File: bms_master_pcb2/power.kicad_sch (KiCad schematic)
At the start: 10 parts, among them U501 AP63205WU, U502 AP2112K-3.3

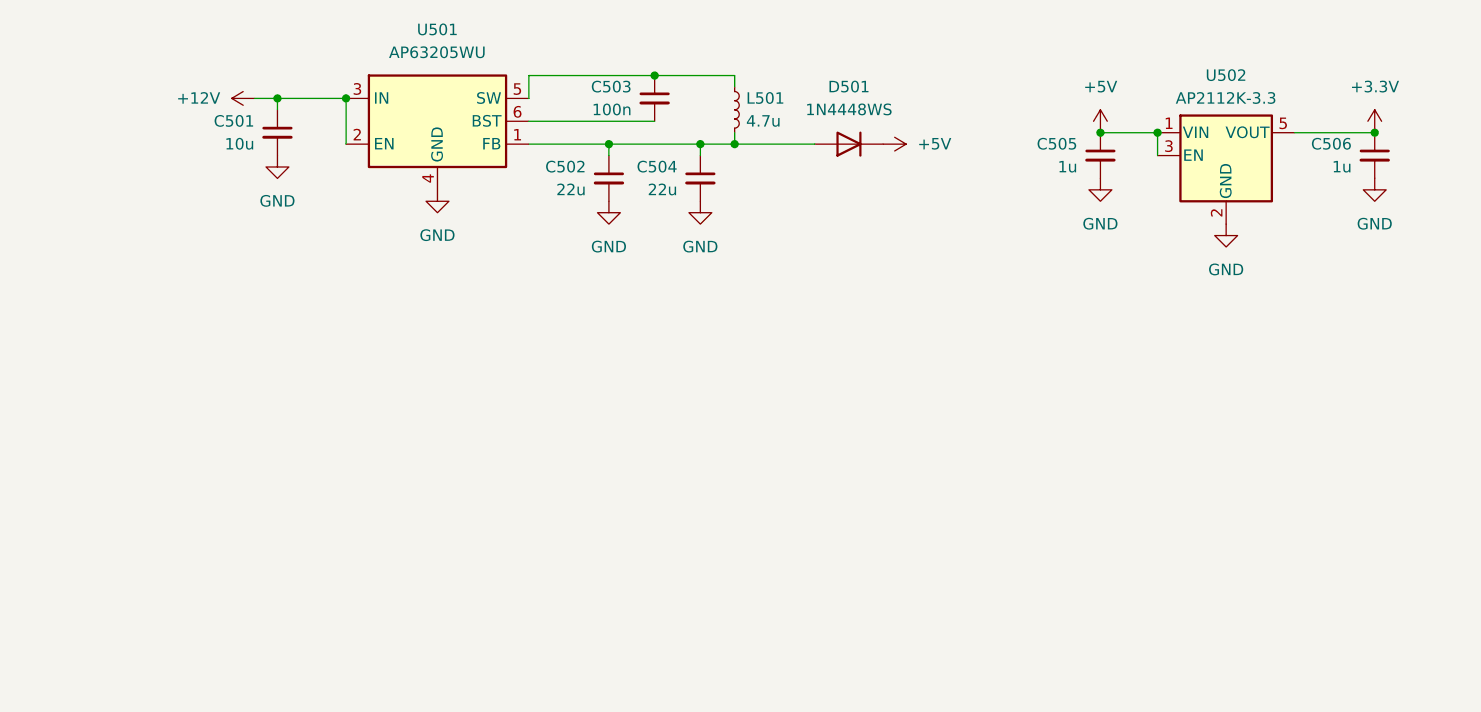
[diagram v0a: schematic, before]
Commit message: Add files via upload
almost done with the PCB layout. Harrison needs to fix routing on the differential pairs
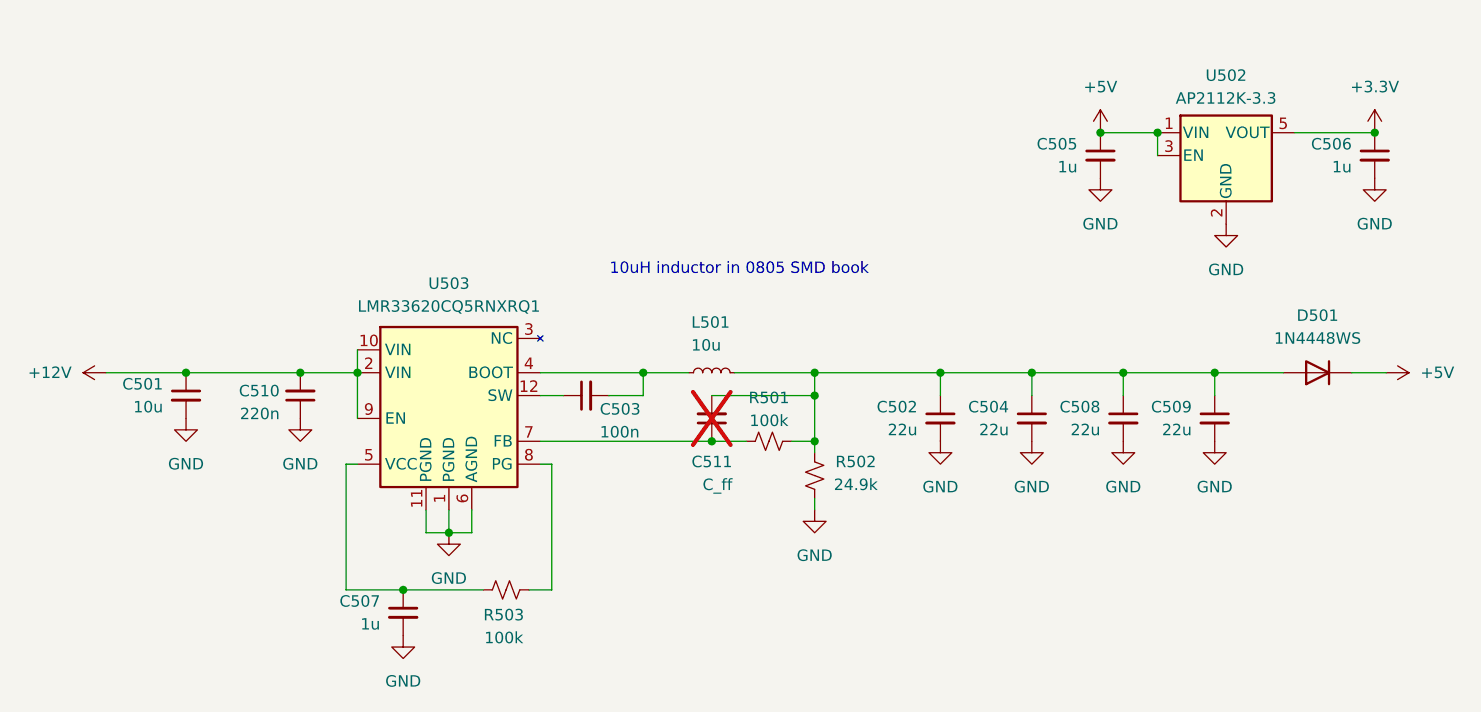
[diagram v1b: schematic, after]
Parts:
- removed U501: AP63205WU, Package_TO_SOT_SMD:TSOT-23-6, symbol Regulator_Switching:AP63205WU
- added C507: 1u, Capacitor_SMD:C_0805_2012Metric_Pad1.18x1.45mm_HandSolder, symbol Device:C_Small
- added C508, C509: 22u, Capacitor_SMD:C_0805_2012Metric_Pad1.18x1.45mm_HandSolder, symbol Device:C_Small
- added C510: 220n, Capacitor_SMD:C_0603_1608Metric_Pad1.08x0.95mm_HandSolder, symbol Device:C_Small
- added C511: C_ff, Capacitor_SMD:C_0603_1608Metric_Pad1.08x0.95mm_HandSolder, symbol Device:C_Small
- added R501, R503: 100k, Resistor_SMD:R_0603_1608Metric_Pad0.98x0.95mm_HandSolder, symbol Device:R_Small_US
- added R502: 24.9k, Resistor_SMD:R_0603_1608Metric_Pad0.98x0.95mm_HandSolder, symbol Device:R_Small_US
- added U503: LMR33620CQ5RNXRQ1, bms_master_pcb2:RNX0012B, symbol Regulator_Switching:LMR33620CDDA
- C501, C502, C504, C505, C506: footprint (none) -> Capacitor_SMD:C_0805_2012Metric_Pad1.18x1.45mm_HandSolder
- C503: footprint (none) -> Capacitor_SMD:C_0603_1608Metric_Pad1.08x0.95mm_HandSolder
- D501: footprint Diode_SMD:D_SOD-323 -> Diode_SMD:D_SOD-323_HandSoldering
- L501: value 4.7u -> 10u; footprint (none) -> Inductor_SMD:L_0805_2012Metric_Pad1.05x1.20mm_HandSolder
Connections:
- net +12V: now also C510.2, U503.10 (VIN), U503.2 (VIN), U503.9 (GND)
- net GND: now also C507.2, C508.2, C509.2, C510.1, R502.2, U503.1 (PGND), U503.11 (PGND), U503.6 (AGND), U503.9 (GND)
- net at C503.1: now also U503.12 (SW); no longer L501.1
- net at C503.2: now also L501.1, U503.4 (BOOT)
- net at C502.1, C504.1, D501.2 (A)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: now also C508.1, C509.1, C511.2, R501.2, R502.1
- new net: C507.1, R503.1, U503.5 (VCC)
- new net: C511.1, R501.1, U503.7 (FB)
- new net: R503.2, U503.8 (PG)
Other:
- note added: "10uH inductor in 0805 SMD book"
- moved on the sheet: C501, C502, C503, C504, D501, L501
